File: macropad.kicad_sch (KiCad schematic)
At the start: 63 parts, among them J1 USB_C_Receptacle_USB2.0, J3 Conn_01x03, J6 Conn_01x04_Pin, J7 Conn_01x02_Pin, J9 Conn_01x02_Pin, SW1 SW_Push, SW3 SW_Push, SW4 SW_Push, SW5 SW_Push, SW6 RotaryEncoder_Switch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

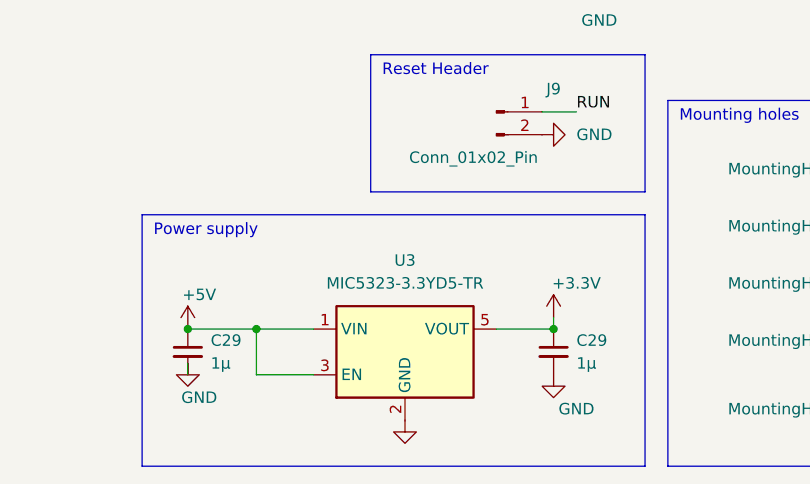
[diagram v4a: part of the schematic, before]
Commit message: Minor cleanups. Made the mounting hole distances round numbers, cleaned up a few traces.
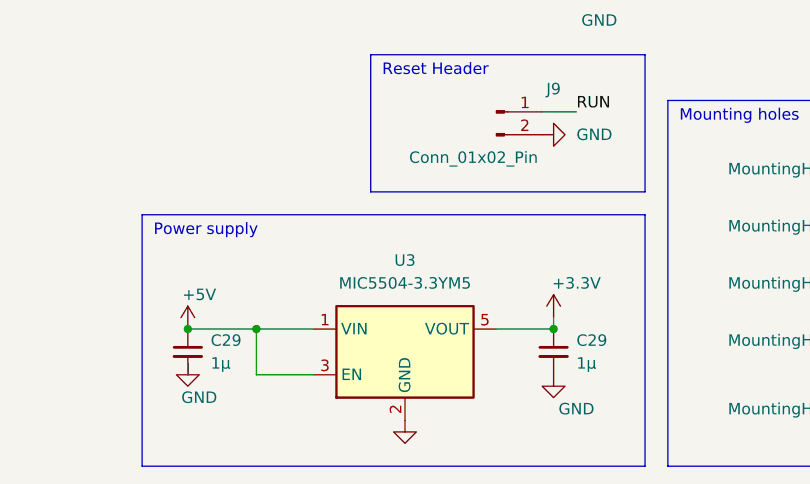
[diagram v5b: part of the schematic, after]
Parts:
- LED1, LED2, LED3, LED4, LED5: LCSC C5200774 -> C5149201
- SW1: LCSC (none) -> C5333465
- SW3, SW4, SW5, SW7: LCSC C5333465 -> (none)
- U2: LCSC C395484 -> C2843335
- U3: value MIC5323-3.3YD5-TR -> MIC5504-3.3YM5; LCSC C512211 -> C88419
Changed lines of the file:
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@@
       (effects (font (size 1.27 1.27)) hide)
     )
-    (property "LCSC" "C5200774" (at 234.95 125.73 0)
+    (property "LCSC" "C5149201" (at 234.95 125.73 0)
       (effects (font (size 1.27 1.27)) hide)
     )
@@
       (effects (font (size 1.27 1.27)) hide)
     )
-    (property "LCSC" "C5200774" (at 199.39 125.73 0)
+    (property "LCSC" "C5149201" (at 199.39 125.73 0)
       (effects (font (size 1.27 1.27)) hide)
     )
@@
       (effects (font (size 1.27 1.27)) hide)
     )
-    (property "LCSC" "C5200774" (at 181.61 125.73 0)
+    (property "LCSC" "C5149201" (at 181.61 125.73 0)
       (effects (font (size 1.27 1.27)) hide)
     )
@@
       (effects (font (size 1.27 1.27)) hide)
     )
-    (property "LCSC" "C395484" (at 16.51 76.2 0)
+    (property "LCSC" "C2843335" (at 16.51 76.2 0)
       (effects (font (size 1.27 1.27)) hide)
     )
@@
       (effects (font (size 1.27 1.27)) hide)
     )
-    (property "LCSC" "C5200774" (at 252.73 125.73 0)
+    (property "LCSC" "C5149201" (at 252.73 125.73 0)
       (effects (font (size 1.27 1.27)) hide)
     )
@@
       (effects (font (size 1.27 1.27)))
     )
-    (property "Value" "MIC5323-3.3YD5-TR" (at 60.96 175.26 0)
+    (property "Value" "MIC5504-3.3YM5" (at 60.96 175.26 0)
       (effects (font (size 1.27 1.27)))
     )
@@
       (effects (font (size 1.27 1.27)) (justify left top) hide)
     )
-    (property "LCSC" "C512211" (at 74.93 175.26 0)
+    (property "LCSC" "C88419" (at 74.93 175.26 0)
       (effects (font (size 1.27 1.27)) hide)
     )
@@
       (effects (font (size 1.27 1.27)) hide)
     )
-    (property "LCSC" "C5333465" (at 207.01 144.78 0)
-      (effects (font (size 1.27 1.27)) hide)
-    )
     (pin "1")
     (pin "2")
@@
       (effects (font (size 1.27 1.27)) hide)
     )
-    (property "LCSC" "C5333465" (at 177.8 144.78 0)
-      (effects (font (size 1.27 1.27)) hide)
-    )
     (pin "1")
     (pin "2")
@@
       (effects (font (size 1.27 1.27)) hide)
     )
+    (property "LCSC" "C5333465" (at 38.1 44.45 0)
+      (effects (font (size 1.27 1.27)) hide)
+    )
     (pin "1")
     (pin "2")
@@
       (effects (font (size 1.27 1.27)) hide)
     )
-    (property "LCSC" "C5200774" (at 217.17 125.73 0)
+    (property "LCSC" "C5149201" (at 217.17 125.73 0)
       (effects (font (size 1.27 1.27)) hide)
     )
@@
       (effects (font (size 1.27 1.27)) hide)
     )
-    (property "LCSC" "C5333465" (at 193.04 144.78 0)
-      (effects (font (size 1.27 1.27)) hide)
-    )
     (pin "1")
     (pin "2")
@@
       (effects (font (size 1.27 1.27)) hide)
     )
-    (property "LCSC" "C5333465" (at 223.52 144.78 0)
-      (effects (font (size 1.27 1.27)) hide)
-    )

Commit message: Modify EC11 footprint to allow SMT parts. Add resistors to the LED data lines.
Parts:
- added R15: 330, Resistor_SMD:R_0402_1005Metric, symbol Device:R_Small
- H1, H3, H4: footprint MountingHole:MountingHole_3.2mm_M3 -> MountingHole:MountingHole_3.2mm_M3_Pad_Via; symbol Mechanical:MountingHole -> Mechanical:MountingHole_Pad
- H2: footprint MountingHole:MountingHole_2.2mm_M2 -> MountingHole:MountingHole_2.2mm_M2_Pad_Via; symbol Mechanical:MountingHole -> Mechanical:MountingHole_Pad
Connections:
- net GND: now also H1.1, H2.1, H3.1, H4.1, H4.1
- net at LED1.3 (DIN): now also R15.1; no longer U6.4 (B)
- new net: R15.2, U6.4 (B)
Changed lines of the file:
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@@
   (junction (at 115.57 31.75) (diameter 0) (color 0 0 0 0)
   )
+  (junction (at 118.11 176.53) (diameter 0) (color 0 0 0 0)
+  )
   (junction (at 246.38 100.33) (diameter 0) (color 0 0 0 0)
   )
@@
   (junction (at 105.41 22.86) (diameter 0) (color 0 0 0 0)
   )
+  (junction (at 118.11 182.88) (diameter 0) (color 0 0 0 0)
+  )
   (junction (at 156.21 31.75) (diameter 0) (color 0 0 0 0)
   )
@@
   (junction (at 57.15 128.27) (diameter 0) (color 0 0 0 0)
   )
+  (junction (at 118.11 189.23) (diameter 0) (color 0 0 0 0)
+  )
   (junction (at 77.47 180.34) (diameter 0) (color 0 0 0 0)
   )
@@
   (junction (at 68.58 20.32) (diameter 0) (color 0 0 0 0)
   )
+  (junction (at 118.11 170.18) (diameter 0) (color 0 0 0 0)
+  )
   (junction (at 124.46 64.77) (diameter 0) (color 0 0 0 0)
   )
@@
     (stroke (width 0) (type default))
   )
+  (wire (pts (xy 118.11 176.53) (xy 118.11 182.88))
+    (stroke (width 0) (type default))
+  )
   (wire (pts (xy 43.18 63.5) (xy 43.18 69.85))
     (stroke (width 0) (type default))
   )
+  (wire (pts (xy 118.11 163.83) (xy 118.11 170.18))
+    (stroke (width 0) (type default))
+  )
   (wire (pts (xy 218.44 49.53) (xy 224.79 49.53))
     (stroke (width 0) (type default))
@@
     (stroke (width 0) (type default))
   )
-  (wire (pts (xy 166.37 22.86) (xy 166.37 25.4))
+  (wire (pts (xy 115.57 176.53) (xy 118.11 176.53))
     (stroke (width 0) (type default))
   )
-  (wire (pts (xy 162.56 118.11) (xy 167.64 118.11))
+  (wire (pts (xy 166.37 22.86) (xy 166.37 25.4))
     (stroke (width 0) (type default))
   )
@@
     (stroke (width 0) (type default))
   )
+  (wire (pts (xy 118.11 182.88) (xy 118.11 189.23))
+    (stroke (width 0) (type default))
+  )
   (wire (pts (xy 222.25 63.5) (xy 218.44 63.5))
     (stroke (width 0) (type default))
   )
+  (wire (pts (xy 118.11 170.18) (xy 118.11 176.53))
+    (stroke (width 0) (type default))
+  )
   (wire (pts (xy 162.56 67.31) (xy 168.91 67.31))
     (stroke (width 0) (type default))
@@
     (stroke (width 0) (type default))
   )
+  (wire (pts (xy 118.11 189.23) (xy 118.11 191.77))
+    (stroke (width 0) (type default))
+  )
   (wire (pts (xy 175.26 99.06) (xy 175.26 100.33))
     (stroke (width 0) (type default))
@@
     (stroke (width 0) (type default))
   )
+  (wire (pts (xy 115.57 189.23) (xy 118.11 189.23))
+    (stroke (width 0) (type default))
+  )
   (wire (pts (xy 80.01 44.45) (xy 80.01 39.37))
     (stroke (width 0) (type default))
@@
     (stroke (width 0) (type default))
   )
+  (wire (pts (xy 115.57 170.18) (xy 118.11 170.18))
+    (stroke (width 0) (type default))
+  )
   (wire (pts (xy 124.46 60.96) (xy 124.46 64.77))
     (stroke (width 0) (type default))
@@
     (stroke (width 0) (type default))
   )
+  (wire (pts (xy 115.57 182.88) (xy 118.11 182.88))
+    (stroke (width 0) (type default))
+  )
   (wire (pts (xy 220.98 44.45) (xy 229.87 44.45))
     (stroke (width 0) (type default))
@@
     (stroke (width 0) (type default))
   )
+  (wire (pts (xy 115.57 163.83) (xy 118.11 163.83))
+    (stroke (width 0) (type default))
+  )
   (wire (pts (xy 157.48 114.3) (xy 162.56 114.3))
     (stroke (width 0) (type default))
@@
     )
   )
+  (symbol (lib_id "Device:R_Small") (at 165.1 118.11 270) (unit 1)
+    (in_bom yes) (on_board yes) (dnp no) (fields_autoplaced)
+    (property "Reference" "R15" (at 165.1 113.03 90)
+      (effects (font (size 1.27 1.27)))
+    )
+    (property "Value" "330" (at 165.1 115.57 90)
+      (effects (font (size 1.27 1.27)))
+    )
+    (property "Footprint" "Resistor_SMD:R_0402_1005Metric" (at 165.1 118.11 0)
+      (effects (font (size 1.27 1.27)) hide)
+    )
+    (property "Datasheet" "~" (at 165.1 118.11 0)
+      (effects (font (size 1.27 1.27)) hide)
+    )
+    (property "LCSC" "C25104" (at 165.1 113.03 0)
+      (effects (font (size 1.27 1.27)) hide)
+    )
+    (pin "1")
+    (pin "2")
+    (instances
+      (project "trackpad"
+        (path "/3796446b-0052-4d89-b512-07a2e9135d0d/2780c9a8-e5e0-42e8-93d7-9eb6f8aa439b"
+          (reference "R15") (unit 1)
+        )
+        (path "/3796446b-0052-4d89-b512-07a2e9135d0d/efc97fde-28db-4fd6-89b1-84dafa779b4e"
+          (reference "R18") (unit 1)
+        )
+      )
+    )
+  )
   (symbol (lib_id "Device:C_Small") (at 135.89 27.94 0) (unit 1)
     (in_bom yes) (on_board yes) (dnp no) (fields_autoplaced)
@@
     )
   )
-  (symbol (lib_id "Mechanical:MountingHole") (at 113.03 163.83 90) (unit 1)
+  (symbol (lib_id "Mechanical:MountingHole_Pad") (at 113.03 163.83 90) (unit 1)
     (in_bom yes) (on_board yes) (dnp no)
     (property "Reference" "H1" (at 107.95 165.1 90)
@@
       (effects (font (size 1.27 1.27)))
     )
-    (property "Footprint" "MountingHole:MountingHole_3.2mm_M3" (at 113.03 163.83 0)
+    (property "Footprint" "MountingHole:MountingHole_3.2mm_M3_Pad_Via" (at 113.03 163.83 0)
       (effects (font (size 1.27 1.27)) hide)
     )
@@
       (effects (font (size 1.27 1.27)) hide)
     )
+    (pin "1")
     (instances
       (project "trackpad"
@@
     )
   )
-  (symbol (lib_id "Mechanical:MountingHole") (at 113.03 176.53 90) (unit 1)
+  (symbol (lib_id "Mechanical:MountingHole_Pad") (at 113.03 176.53 90) (unit 1)
     (in_bom yes) (on_board yes) (dnp no)
     (property "Reference" "H3" (at 107.95 177.8 90)
@@
       (effects (font (size 1.27 1.27)))
     )
-    (property "Footprint" "MountingHole:MountingHole_3.2mm_M3" (at 113.03 176.53 0)
+    (property "Footprint" "MountingHole:MountingHole_3.2mm_M3_Pad_Via" (at 113.03 176.53 0)
       (effects (font (size 1.27 1.27)) hide)
     )
@@
       (effects (font (size 1.27 1.27)) hide)
     )
+    (pin "1")
     (instances
       (project "trackpad"
@@
     )
   )
-  (symbol (lib_id "Mechanical:MountingHole") (at 113.03 182.88 90) (unit 1)
+  (symbol (lib_id "Mechanical:MountingHole_Pad") (at 113.03 182.88 90) (unit 1)
     (in_bom yes) (on_board yes) (dnp no)
     (property "Reference" "H4" (at 107.95 184.15 90)
@@
       (effects (font (size 1.27 1.27)))
     )
-    (property "Footprint" "MountingHole:MountingHole_3.2mm_M3" (at 113.03 182.88 0)
+    (property "Footprint" "MountingHole:MountingHole_3.2mm_M3_Pad_Via" (at 113.03 182.88 0)
       (effects (font (size 1.27 1.27)) hide)
     )
@@
       (effects (font (size 1.27 1.27)) hide)
     )
+    (pin "1")
     (instances
       (project "trackpad"
@@
     )
   )
+  (symbol (lib_id "power:GND") (at 118.11 191.77 0) (unit 1)
+    (in_bom yes) (on_board yes) (dnp no)
+    (property "Reference" "#PWR032" (at 118.11 198.12 0)
+      (effects (font (size 1.27 1.27)) hide)
+    )
+    (property "Value" "GND" (at 120.65 195.58 0)
+      (effects (font (size 1.27 1.27)))
+    )
+    (property "Footprint" "" (at 118.11 191.77 0)
+      (effects (font (size 1.27 1.27)) hide)
+    )
+    (property "Datasheet" "" (at 118.11 191.77 0)
+      (effects (font (size 1.27 1.27)) hide)
+    )
+    (pin "1")
+    (instances
+      (project "trackpad"
+        (path "/3796446b-0052-4d89-b512-07a2e9135d0d"
+          (reference "#PWR032") (unit 1)
+        )
+        (path "/3796446b-0052-4d89-b512-07a2e9135d0d/efc97fde-28db-4fd6-89b1-84dafa779b4e"
+          (reference "#PWR083") (unit 1)
+        )
+      )
+    )
+  )
   (symbol (lib_id "power:GND") (at 127 149.86 0) (unit 1)
     (in_bom yes) (on_board yes) (dnp no) (fields_autoplaced)
@@
     )
   )
-  (symbol (lib_id "Mechanical:MountingHole") (at 113.03 189.23 90) (unit 1)
+  (symbol (lib_id "Mechanical:MountingHole_Pad") (at 113.03 189.23 90) (unit 1)
     (in_bom yes) (on_board yes) (dnp no)
     (property "Reference" "H4" (at 107.95 191.77 90)
@@
       (effects (font (size 1.27 1.27)))
     )
-    (property "Footprint" "MountingHole:MountingHole_3.2mm_M3" (at 113.03 189.23 0)
+    (property "Footprint" "MountingHole:MountingHole_3.2mm_M3_Pad_Via" (at 113.03 189.23 0)
       (effects (font (size 1.27 1.27)) hide)
     )
@@
       (effects (font (size 1.27 1.27)) hide)
     )
+    (pin "1")
     (instances
       (project "trackpad"
@@
     )
   )
-  (symbol (lib_id "Mechanical:MountingHole") (at 113.03 170.18 90) (unit 1)
+  (symbol (lib_id "Mechanical:MountingHole_Pad") (at 113.03 170.18 90) (unit 1)
     (in_bom yes) (on_board yes) (dnp no)
     (property "Reference" "H2" (at 107.95 171.45 90)
@@
       (effects (font (size 1.27 1.27)))
     )
-    (property "Footprint" "MountingHole:MountingHole_2.2mm_M2" (at 113.03 170.18 0)
+    (property "Footprint" "MountingHole:MountingHole_2.2mm_M2_Pad_Via" (at 113.03 170.18 0)
       (effects (font (size 1.27 1.27)) hide)
     )
@@
       (effects (font (size 1.27 1.27)) hide)
     )
+    (pin "1")
     (instances
       (project "trackpad"

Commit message: Fix DRC issue and add VCC warning.
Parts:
- R15: LCSC C25104 -> (none)
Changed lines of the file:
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@@
-      (effects (font (size 1.27 1.27)) hide)
-    )
-    (property "LCSC" "C25104" (at 165.1 113.03 0)
       (effects (font (size 1.27 1.27)) hide)
     )

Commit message: Minor tweaks
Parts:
- removed R4, R5: 4.7k, Resistor_SMD:R_1206_3216Metric_Pad1.30x1.75mm_HandSolder, symbol Device:R_Small
- added C5: 100n, Capacitor_SMD:C_0402_1005Metric, symbol Device:C_Small
- C29: LCSC C1525 -> C52923
- R15: LCSC (none) -> C25104
- SW1: LCSC C5333465 -> C221821
- SW6: LCSC C5333465 -> (none)
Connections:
- net +3.3V: now also C5.2
- net GND: now also C5.1
- net SCL: now also U1.13 (GPIO10); no longer U1.7 (GPIO5)
- net SDA: now also U1.12 (GPIO9); no longer U1.6 (GPIO4)
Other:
- moved on the sheet: SW3, SW4, SW5, SW7, SW8
